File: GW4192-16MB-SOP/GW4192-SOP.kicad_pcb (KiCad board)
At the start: 4 copper layers, 88.9 x 20.8 mm, 14 parts, among them J1 DRAM-SIMM-30, U1 KM44C16104, U2 KM44C16104

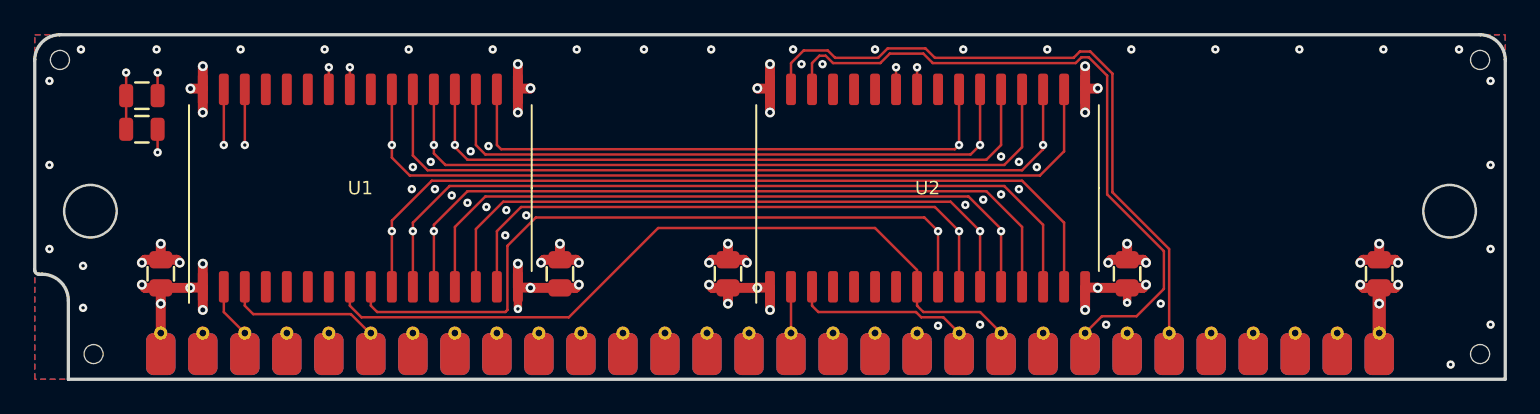
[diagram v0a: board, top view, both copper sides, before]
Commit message: Update to KiCAD 6
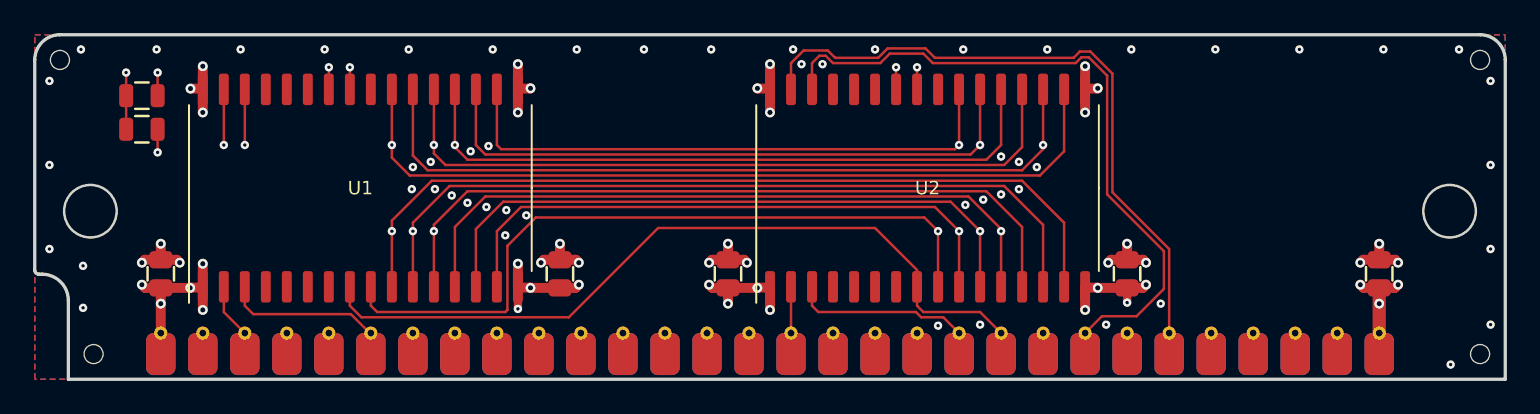
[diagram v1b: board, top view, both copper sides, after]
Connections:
- net /~CASP~ renamed /~{CASP}
- net /~CAS~ renamed /~{CAS}
- net /~OE~ renamed /~{OE}
- net /~RAS~ renamed /~{RAS}
- net /~WE~ renamed /~{WE}
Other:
- net class Default removed
